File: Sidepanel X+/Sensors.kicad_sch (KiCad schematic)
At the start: 8 parts, among them IC1 TMP112AQDRLRQ1, U1 GUVA-C32SM

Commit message: Review Ready for V2.0
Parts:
- IC1: footprint SamacSys:SOTFL50P160X60-6N -> Package_TO_SOT_SMD:SOT-563
- U1: footprint USER_Optic:OLGA 2mm x 2,3mm -> Package_SO:SO-4_4.4x3.6mm_P2.54mm
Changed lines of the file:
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@@
     (property "Reference" "U1" (id 0) (at 60.96 34.29 0))
     (property "Value" "GUVA-C32SM" (id 1) (at 60.96 36.83 0))
-    (property "Footprint" "USER_Optic:OLGA 2mm x 2,3mm" (id 2) (at 60.96 45.72 0)
+    (property "Footprint" "Package_SO:SO-4_4.4x3.6mm_P2.54mm" (id 2) (at 60.96 45.72 0)
       (effects (font (size 1.27 1.27)) hide)
     )
@@
     (property "Reference" "IC1" (id 0) (at 142.24 34.29 0))
     (property "Value" "TMP112AQDRLRQ1" (id 1) (at 142.24 36.83 0))
-    (property "Footprint" "SamacSys:SOTFL50P160X60-6N" (id 2) (at 153.67 39.37 0)
+    (property "Footprint" "Package_TO_SOT_SMD:SOT-563" (id 2) (at 153.67 39.37 0)
       (effects (font (size 1.27 1.27)) (justify left) hide)
     )

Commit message: Further fixes, still some open
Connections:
- net VBAT is gone; now on net +3V3: C1.1, U1.4 (VCC)
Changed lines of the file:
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@@
   (junction (at 165.1 39.37) (diameter 0) (color 0 0 0 0)
+  )
+  (junction (at 50.8 34.29) (diameter 0) (color 0 0 0 0)
   )
   (junction (at 71.12 41.91) (diameter 0) (color 0 0 0 0)
@@
     (stroke (width 0) (type default) (color 0 0 0 0))
   )
-  (wire (pts (xy 48.26 46.99) (xy 50.8 46.99))
+  (wire (pts (xy 27.94 46.99) (xy 50.8 46.99))
     (stroke (width 0) (type default) (color 0 0 0 0))
   )
   (wire (pts (xy 165.1 45.72) (xy 165.1 46.99))
+    (stroke (width 0) (type default) (color 0 0 0 0))
+  )
+  (wire (pts (xy 50.8 34.29) (xy 50.8 35.56))
     (stroke (width 0) (type default) (color 0 0 0 0))
   )
@@
   )
   (wire (pts (xy 124.46 41.91) (xy 127 41.91))
+    (stroke (width 0) (type default) (color 0 0 0 0))
+  )
+  (wire (pts (xy 27.94 46.99) (xy 27.94 34.29))
     (stroke (width 0) (type default) (color 0 0 0 0))
   )
@@
     (stroke (width 0) (type default) (color 0 0 0 0))
   )
+  (wire (pts (xy 27.94 34.29) (xy 50.8 34.29))
+    (stroke (width 0) (type default) (color 0 0 0 0))
+  )
   (wire (pts (xy 119.38 41.91) (xy 124.46 41.91))
     (stroke (width 0) (type default) (color 0 0 0 0))
@@
     (stroke (width 0) (type default) (color 0 0 0 0))
   )
-  (wire (pts (xy 50.8 33.02) (xy 50.8 35.56))
+  (wire (pts (xy 50.8 33.02) (xy 50.8 34.29))
     (stroke (width 0) (type default) (color 0 0 0 0))
   )
@@
     (stroke (width 0) (type default) (color 0 0 0 0))
   )
-  (hierarchical_label "VBAT" (shape input) (at 48.26 46.99 180)
-    (effects (font (size 1.27 1.27)) (justify right))
-  )
-  (hierarchical_label "VBAT" (shape input) (at 48.26 46.99 180)
-    (effects (font (size 1.27 1.27)) (justify right))
-  )
   (hierarchical_label "SDA_TMP" (shape bidirectional) (at 166.37 46.99 0)

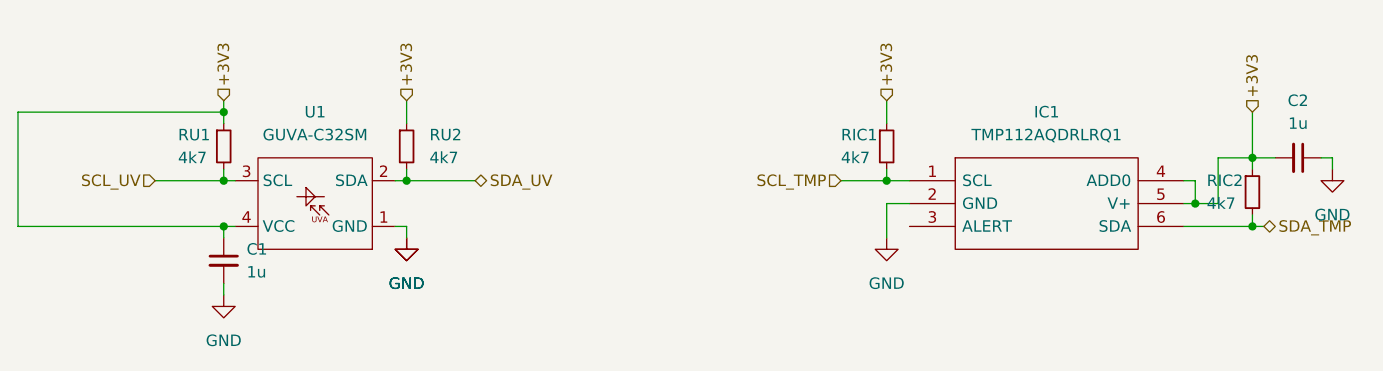
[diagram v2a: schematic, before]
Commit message: Fixed some DRC errors.
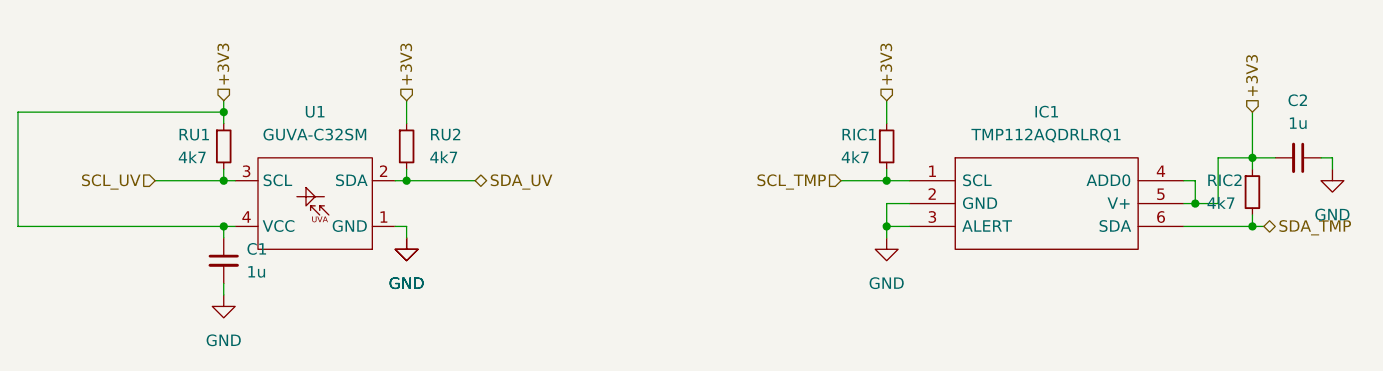
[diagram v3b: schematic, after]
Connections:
- net GND: now also IC1.3 (ALERT)
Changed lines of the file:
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@@
   (junction (at 165.1 39.37) (diameter 0) (color 0 0 0 0)
+  )
+  (junction (at 124.46 46.99) (diameter 0) (color 0 0 0 0)
   )
   (junction (at 50.8 34.29) (diameter 0) (color 0 0 0 0)
@@
   )
   (wire (pts (xy 50.8 34.29) (xy 50.8 35.56))
+    (stroke (width 0) (type default) (color 0 0 0 0))
+  )
+  (wire (pts (xy 124.46 46.99) (xy 124.46 48.26))
     (stroke (width 0) (type default) (color 0 0 0 0))
   )
@@
     (stroke (width 0) (type default) (color 0 0 0 0))
   )
+  (wire (pts (xy 124.46 46.99) (xy 127 46.99))
+    (stroke (width 0) (type default) (color 0 0 0 0))
+  )
   (wire (pts (xy 50.8 41.91) (xy 52.07 41.91))
     (stroke (width 0) (type default) (color 0 0 0 0))
@@
     (stroke (width 0) (type default) (color 0 0 0 0))
   )
-  (wire (pts (xy 124.46 44.45) (xy 124.46 48.26))
+  (wire (pts (xy 124.46 44.45) (xy 124.46 46.99))
     (stroke (width 0) (type default) (color 0 0 0 0))
   )

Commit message: Adjusted the panel naming so that it conforms to the coordinate system convention governed by the Cubesat Design Specification.
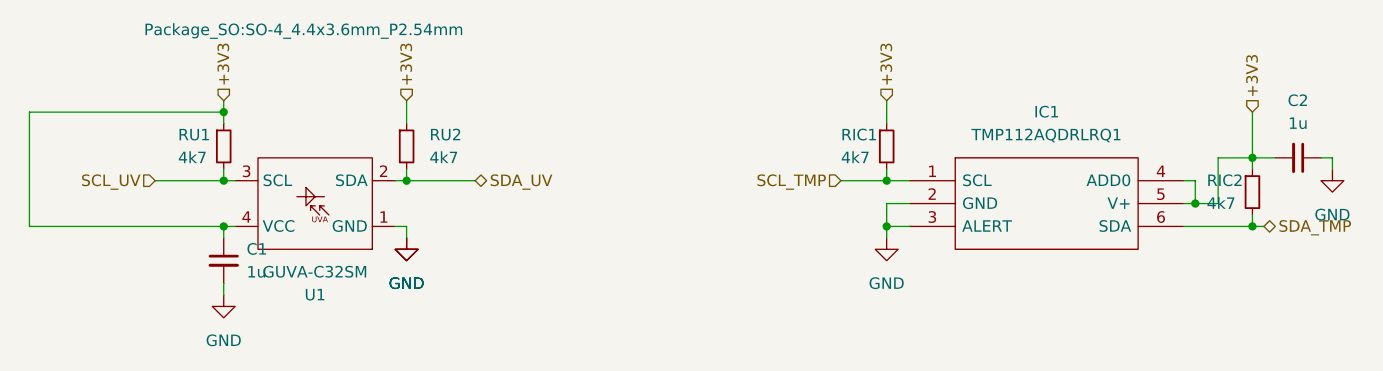
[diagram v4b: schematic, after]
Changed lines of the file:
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@@
   (junction (at 124.46 46.99) (diameter 0) (color 0 0 0 0)
   )
+  (junction (at 71.12 41.91) (diameter 0) (color 0 0 0 0)
+  )
+  (junction (at 124.46 41.91) (diameter 0) (color 0 0 0 0)
+  )
+  (junction (at 165.1 46.99) (diameter 0) (color 0 0 0 0)
+  )
   (junction (at 50.8 34.29) (diameter 0) (color 0 0 0 0)
   )
-  (junction (at 71.12 41.91) (diameter 0) (color 0 0 0 0)
-  )
-  (junction (at 124.46 41.91) (diameter 0) (color 0 0 0 0)
-  )
-  (junction (at 165.1 46.99) (diameter 0) (color 0 0 0 0)
-  )
   (junction (at 50.8 41.91) (diameter 0) (color 0 0 0 0)
   )
@@
     (stroke (width 0) (type default) (color 0 0 0 0))
   )
-  (wire (pts (xy 27.94 46.99) (xy 50.8 46.99))
-    (stroke (width 0) (type default) (color 0 0 0 0))
-  )
   (wire (pts (xy 165.1 45.72) (xy 165.1 46.99))
     (stroke (width 0) (type default) (color 0 0 0 0))
   )
+  (wire (pts (xy 29.21 34.29) (xy 50.8 34.29))
+    (stroke (width 0) (type default) (color 0 0 0 0))
+  )
+  (wire (pts (xy 71.12 40.64) (xy 71.12 41.91))
+    (stroke (width 0) (type default) (color 0 0 0 0))
+  )
+  (wire (pts (xy 124.46 41.91) (xy 127 41.91))
+    (stroke (width 0) (type default) (color 0 0 0 0))
+  )
+  (wire (pts (xy 71.12 41.91) (xy 78.74 41.91))
+    (stroke (width 0) (type default) (color 0 0 0 0))
+  )
+  (wire (pts (xy 157.48 41.91) (xy 158.75 41.91))
+    (stroke (width 0) (type default) (color 0 0 0 0))
+  )
+  (wire (pts (xy 165.1 39.37) (xy 167.64 39.37))
+    (stroke (width 0) (type default) (color 0 0 0 0))
+  )
+  (wire (pts (xy 119.38 41.91) (xy 124.46 41.91))
+    (stroke (width 0) (type default) (color 0 0 0 0))
+  )
+  (wire (pts (xy 166.37 46.99) (xy 165.1 46.99))
+    (stroke (width 0) (type default) (color 0 0 0 0))
+  )
+  (wire (pts (xy 50.8 33.02) (xy 50.8 34.29))
+    (stroke (width 0) (type default) (color 0 0 0 0))
+  )
+  (wire (pts (xy 124.46 40.64) (xy 124.46 41.91))
+    (stroke (width 0) (type default) (color 0 0 0 0))
+  )
+  (wire (pts (xy 69.85 46.99) (xy 71.12 46.99))
+    (stroke (width 0) (type default) (color 0 0 0 0))
+  )
+  (wire (pts (xy 124.46 33.02) (xy 124.46 35.56))
+    (stroke (width 0) (type default) (color 0 0 0 0))
+  )
+  (wire (pts (xy 161.29 44.45) (xy 161.29 39.37))
+    (stroke (width 0) (type default) (color 0 0 0 0))
+  )
+  (wire (pts (xy 165.1 46.99) (xy 157.48 46.99))
+    (stroke (width 0) (type default) (color 0 0 0 0))
+  )
+  (wire (pts (xy 29.21 46.99) (xy 50.8 46.99))
+    (stroke (width 0) (type default) (color 0 0 0 0))
+  )
   (wire (pts (xy 50.8 34.29) (xy 50.8 35.56))
     (stroke (width 0) (type default) (color 0 0 0 0))
   )
+  (wire (pts (xy 50.8 41.91) (xy 52.07 41.91))
+    (stroke (width 0) (type default) (color 0 0 0 0))
+  )
+  (wire (pts (xy 172.72 39.37) (xy 173.99 39.37))
+    (stroke (width 0) (type default) (color 0 0 0 0))
+  )
+  (wire (pts (xy 158.75 41.91) (xy 158.75 44.45))
+    (stroke (width 0) (type default) (color 0 0 0 0))
+  )
+  (wire (pts (xy 50.8 46.99) (xy 50.8 48.26))
+    (stroke (width 0) (type default) (color 0 0 0 0))
+  )
+  (wire (pts (xy 161.29 39.37) (xy 165.1 39.37))
+    (stroke (width 0) (type default) (color 0 0 0 0))
+  )
+  (wire (pts (xy 127 44.45) (xy 124.46 44.45))
+    (stroke (width 0) (type default) (color 0 0 0 0))
+  )
+  (wire (pts (xy 43.18 41.91) (xy 50.8 41.91))
+    (stroke (width 0) (type default) (color 0 0 0 0))
+  )
+  (wire (pts (xy 173.99 39.37) (xy 173.99 40.64))
+    (stroke (width 0) (type default) (color 0 0 0 0))
+  )
+  (wire (pts (xy 158.75 44.45) (xy 161.29 44.45))
+    (stroke (width 0) (type default) (color 0 0 0 0))
+  )
+  (wire (pts (xy 50.8 40.64) (xy 50.8 41.91))
+    (stroke (width 0) (type default) (color 0 0 0 0))
+  )
+  (wire (pts (xy 71.12 46.99) (xy 71.12 48.26))
+    (stroke (width 0) (type default) (color 0 0 0 0))
+  )
+  (wire (pts (xy 29.21 46.99) (xy 29.21 34.29))
+    (stroke (width 0) (type default) (color 0 0 0 0))
+  )
+  (wire (pts (xy 69.85 41.91) (xy 71.12 41.91))
+    (stroke (width 0) (type default) (color 0 0 0 0))
+  )
+  (wire (pts (xy 165.1 34.29) (xy 165.1 39.37))
+    (stroke (width 0) (type default) (color 0 0 0 0))
+  )
+  (wire (pts (xy 165.1 39.37) (xy 165.1 40.64))
+    (stroke (width 0) (type default) (color 0 0 0 0))
+  )
   (wire (pts (xy 124.46 46.99) (xy 124.46 48.26))
     (stroke (width 0) (type default) (color 0 0 0 0))
   )
-  (wire (pts (xy 71.12 40.64) (xy 71.12 41.91))
-    (stroke (width 0) (type default) (color 0 0 0 0))
-  )
-  (wire (pts (xy 124.46 41.91) (xy 127 41.91))
-    (stroke (width 0) (type default) (color 0 0 0 0))
-  )
-  (wire (pts (xy 27.94 46.99) (xy 27.94 34.29))
-    (stroke (width 0) (type default) (color 0 0 0 0))
-  )
-  (wire (pts (xy 71.12 41.91) (xy 78.74 41.91))
-    (stroke (width 0) (type default) (color 0 0 0 0))
-  )
-  (wire (pts (xy 157.48 41.91) (xy 158.75 41.91))
-    (stroke (width 0) (type default) (color 0 0 0 0))
-  )
-  (wire (pts (xy 165.1 39.37) (xy 167.64 39.37))
-    (stroke (width 0) (type default) (color 0 0 0 0))
-  )
-  (wire (pts (xy 27.94 34.29) (xy 50.8 34.29))
-    (stroke (width 0) (type default) (color 0 0 0 0))
-  )
-  (wire (pts (xy 119.38 41.91) (xy 124.46 41.91))
-    (stroke (width 0) (type default) (color 0 0 0 0))
-  )
-  (wire (pts (xy 166.37 46.99) (xy 165.1 46.99))
-    (stroke (width 0) (type default) (color 0 0 0 0))
-  )
-  (wire (pts (xy 50.8 33.02) (xy 50.8 34.29))
-    (stroke (width 0) (type default) (color 0 0 0 0))
-  )
-  (wire (pts (xy 124.46 40.64) (xy 124.46 41.91))
-    (stroke (width 0) (type default) (color 0 0 0 0))
-  )
-  (wire (pts (xy 69.85 46.99) (xy 71.12 46.99))
-    (stroke (width 0) (type default) (color 0 0 0 0))
-  )
-  (wire (pts (xy 124.46 33.02) (xy 124.46 35.56))
-    (stroke (width 0) (type default) (color 0 0 0 0))
-  )
-  (wire (pts (xy 161.29 44.45) (xy 161.29 39.37))
-    (stroke (width 0) (type default) (color 0 0 0 0))
-  )
-  (wire (pts (xy 165.1 46.99) (xy 157.48 46.99))
-    (stroke (width 0) (type default) (color 0 0 0 0))
-  )
-  (wire (pts (xy 124.46 46.99) (xy 127 46.99))
-    (stroke (width 0) (type default) (color 0 0 0 0))
-  )
-  (wire (pts (xy 50.8 41.91) (xy 52.07 41.91))
-    (stroke (width 0) (type default) (color 0 0 0 0))
-  )
-  (wire (pts (xy 172.72 39.37) (xy 173.99 39.37))
-    (stroke (width 0) (type default) (color 0 0 0 0))
-  )
-  (wire (pts (xy 158.75 41.91) (xy 158.75 44.45))
-    (stroke (width 0) (type default) (color 0 0 0 0))
-  )
-  (wire (pts (xy 50.8 46.99) (xy 50.8 48.26))
-    (stroke (width 0) (type default) (color 0 0 0 0))
-  )
-  (wire (pts (xy 161.29 39.37) (xy 165.1 39.37))
-    (stroke (width 0) (type default) (color 0 0 0 0))
-  )
-  (wire (pts (xy 127 44.45) (xy 124.46 44.45))
-    (stroke (width 0) (type default) (color 0 0 0 0))
-  )
-  (wire (pts (xy 43.18 41.91) (xy 50.8 41.91))
-    (stroke (width 0) (type default) (color 0 0 0 0))
-  )
-  (wire (pts (xy 173.99 39.37) (xy 173.99 40.64))
-    (stroke (width 0) (type default) (color 0 0 0 0))
-  )
-  (wire (pts (xy 158.75 44.45) (xy 161.29 44.45))
-    (stroke (width 0) (type default) (color 0 0 0 0))
-  )
-  (wire (pts (xy 50.8 40.64) (xy 50.8 41.91))
-    (stroke (width 0) (type default) (color 0 0 0 0))
-  )
-  (wire (pts (xy 71.12 46.99) (xy 71.12 48.26))
-    (stroke (width 0) (type default) (color 0 0 0 0))
-  )
-  (wire (pts (xy 69.85 41.91) (xy 71.12 41.91))
-    (stroke (width 0) (type default) (color 0 0 0 0))
-  )
-  (wire (pts (xy 165.1 34.29) (xy 165.1 39.37))
-    (stroke (width 0) (type default) (color 0 0 0 0))
-  )
-  (wire (pts (xy 165.1 39.37) (xy 165.1 40.64))
-    (stroke (width 0) (type default) (color 0 0 0 0))
-  )
   (wire (pts (xy 124.46 44.45) (xy 124.46 46.99))
+    (stroke (width 0) (type default) (color 0 0 0 0))
+  )
+  (wire (pts (xy 127 46.99) (xy 124.46 46.99))
     (stroke (width 0) (type default) (color 0 0 0 0))
   )
@@
   )
   (symbol (lib_id "USER_Optic:GUVA-C32SM") (at 60.96 44.45 180) (unit 1)
-    (in_bom yes) (on_board yes) (fields_autoplaced)
-    (property "Reference" "U1" (id 0) (at 60.96 34.29 0))
-    (property "Value" "GUVA-C32SM" (id 1) (at 60.96 36.83 0))
-    (property "Footprint" "Package_SO:SO-4_4.4x3.6mm_P2.54mm" (id 2) (at 60.96 45.72 0)
-      (effects (font (size 1.27 1.27)) hide)
-    )
-    (property "Datasheet" "" (id 3) (at 60.96 45.72 0)
-      (effects (font (size 1.27 1.27)) hide)
-    )
+    (in_bom yes) (on_board yes)
+    (property "Reference" "U1" (id 0) (at 60.96 54.61 0))
+    (property "Value" "GUVA-C32SM" (id 1) (at 60.96 52.07 0))
+    (property "Footprint" "Package_SO:SO-4_4.4x3.6mm_P2.54mm" (id 2) (at 59.69 25.146 0))
+    (property "Datasheet" "" (id 3) (at 60.96 43.18 0)
+      (effects (font (size 1.27 1.27)) hide)
+    )
